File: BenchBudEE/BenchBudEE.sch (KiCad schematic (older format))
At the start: 0 parts

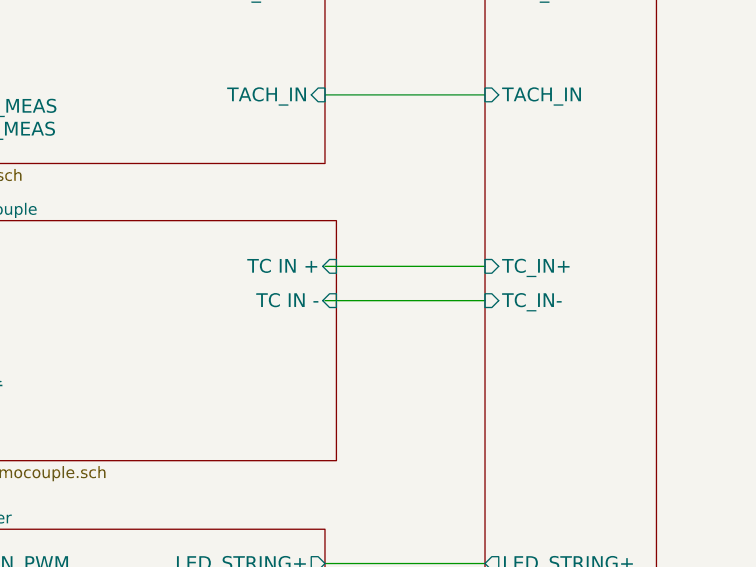
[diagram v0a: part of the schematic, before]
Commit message: Finalizing the system part placement
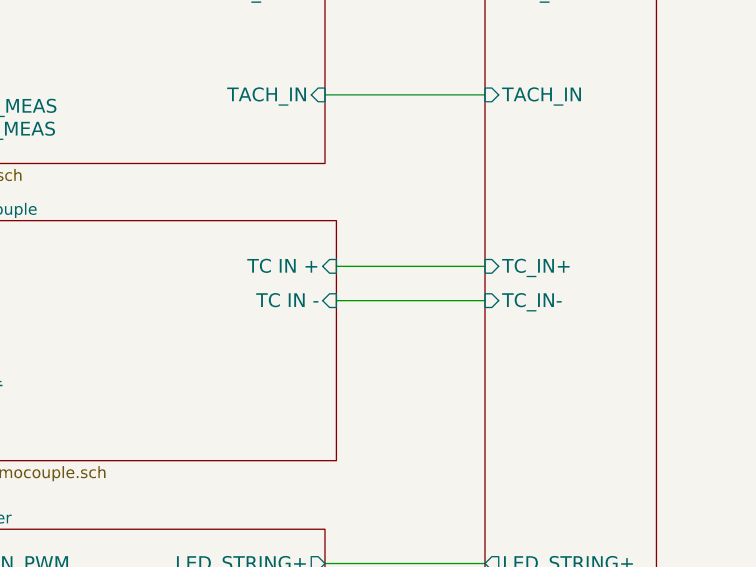
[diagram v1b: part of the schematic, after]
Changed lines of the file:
@@
 $EndSheet
-Wire Wire Line
-	8850 4350 9550 4350
-Wire Wire Line
-	9550 4500 8850 4500
 Wire Wire Line
 	9550 5650 8850 5650
@@
 Wire Wire Line
 	4100 3250 7100 3250
+Wire Wire Line
+	8900 4350 9550 4350
+Wire Wire Line
+	8900 4500 9550 4500
 $EndSCHEMATC
